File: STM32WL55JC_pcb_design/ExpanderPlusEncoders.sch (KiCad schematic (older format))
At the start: 11 parts, among them IC2 CY8C9540A-24PVXIT, J12 Conn_01x10, J13 Conn_01x10, J14 Conn_01x10, J15 Conn_01x10, SW2 SW_MEC_5E

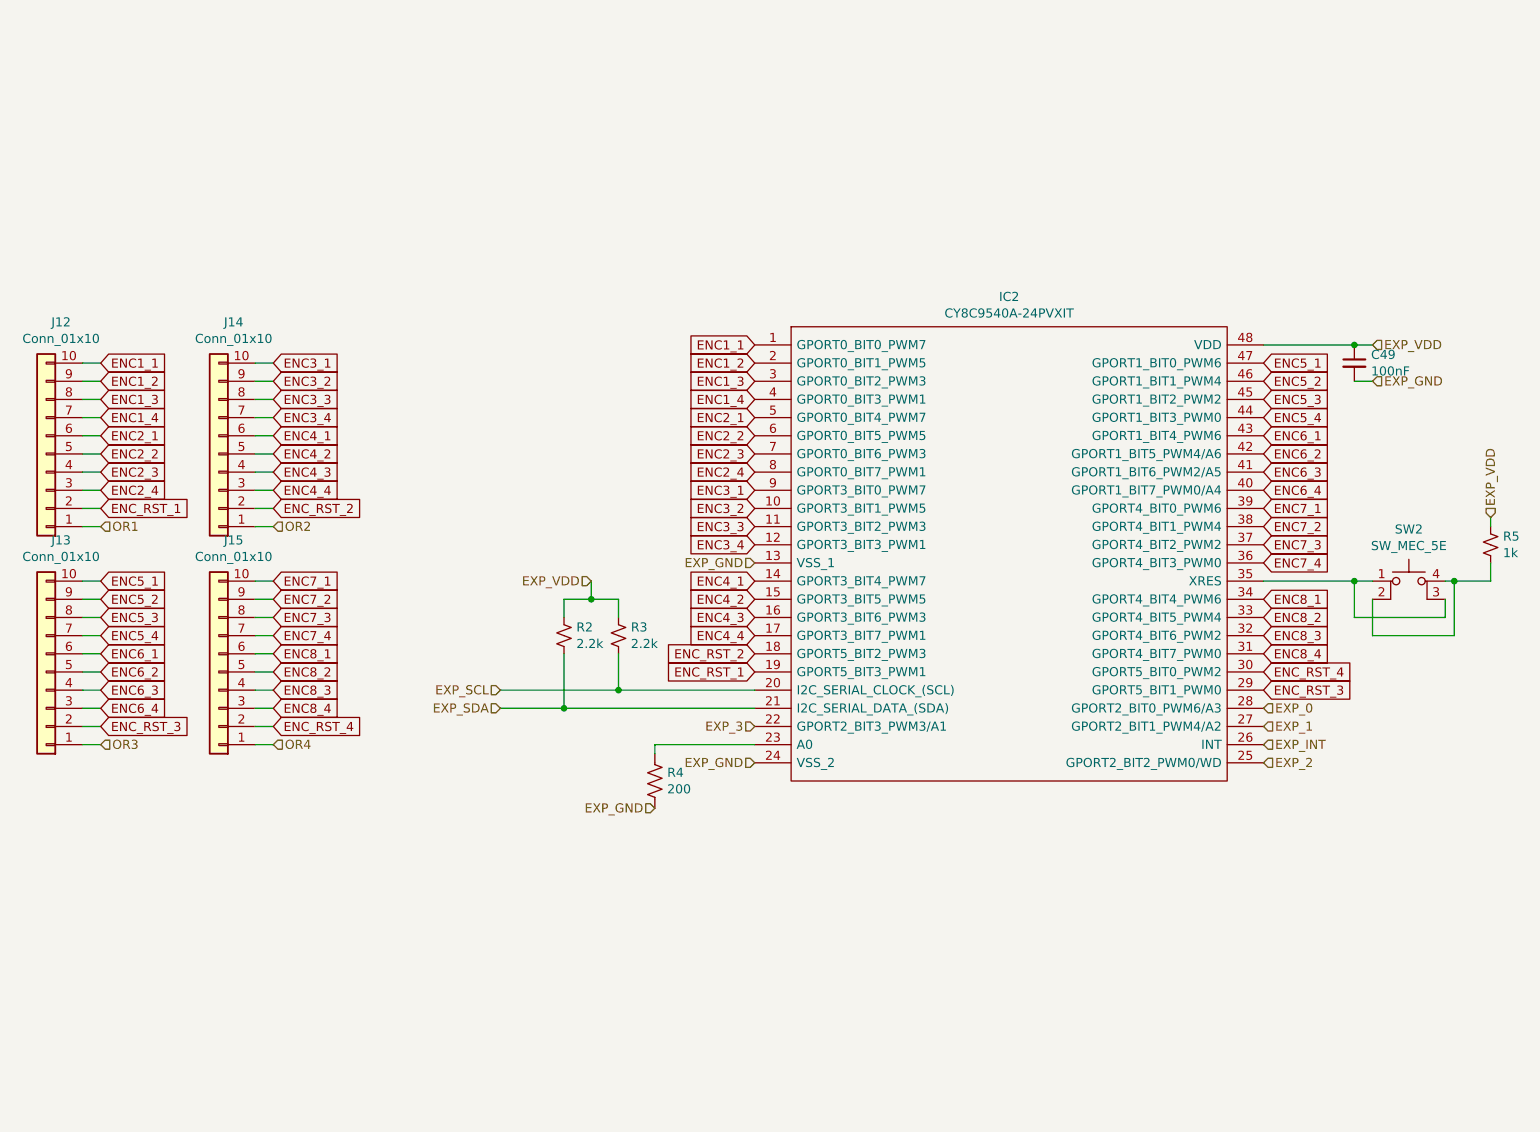
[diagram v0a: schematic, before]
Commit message: Change devices to available ones from JLC
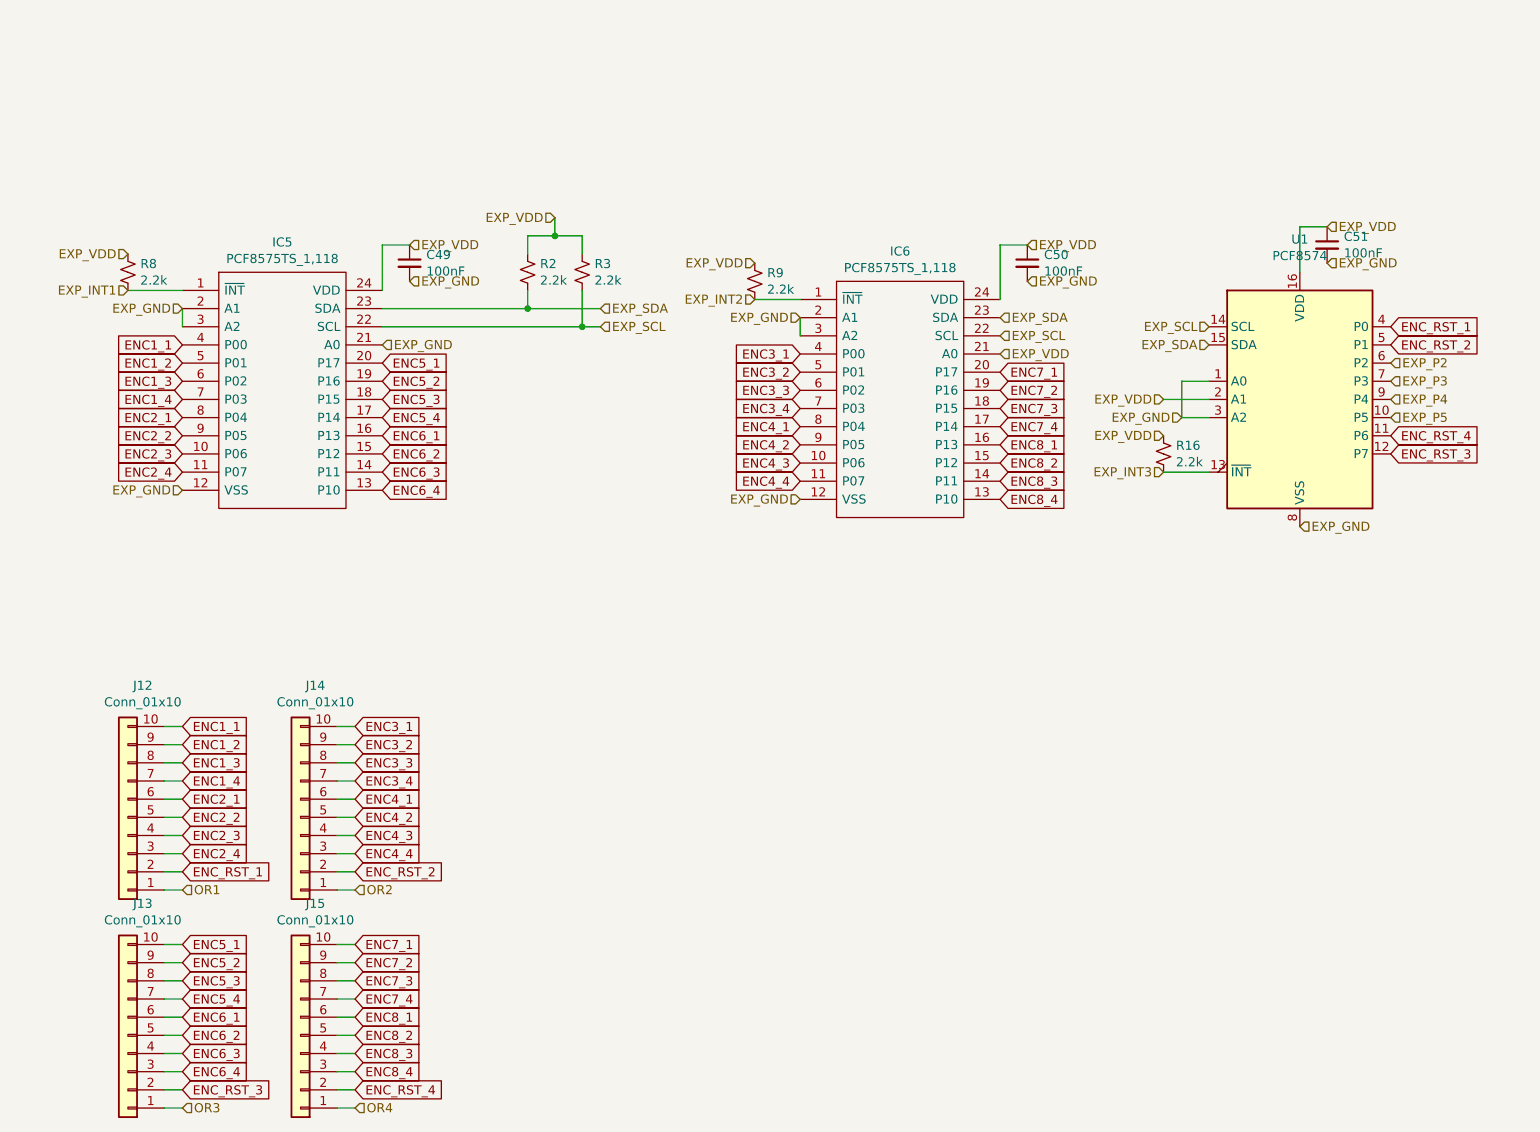
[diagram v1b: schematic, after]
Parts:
- removed IC2: CY8C9540A-24PVXIT, CY8C9540A-24PVXIT:SOP64P1035X279-48N, symbol CY8C9540A-24PVXIT:CY8C9540A-24PVXIT
- removed R4: 200, Resistor_SMD:R_0805_2012Metric, symbol Device:R_US
- removed R5: 1k, Resistor_SMD:R_0805_2012Metric, symbol Device:R_Small_US
- removed SW2: SW_MEC_5E, EVQ-P2F02K:EVQP2V02W, symbol Switch:SW_MEC_5E
- added C50, C51: 100nF, Capacitor_SMD:C_0805_2012Metric, symbol Device:C_Small
- added IC5, IC6: PCF8575TS_1,118, PCF8575TS_1_118:SOP65P775X200-24N, symbol PCF8575TS_1_118:PCF8575TS_1,118
- added R16, R8, R9: 2.2k, Resistor_SMD:R_0805_2012Metric, symbol Device:R_Small_US
- added U1: PCF8574, PCF8574T_3_518:SOIC127P1032X265-16N, symbol Interface_Expansion:PCF8574
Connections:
- net ENC1_1: now also IC5.4 (P00)
- net ENC1_2: now also IC5.5 (P01)
- net ENC1_3: now also IC5.6 (P02)
- net ENC1_4: now also IC5.7 (P03)
- net ENC2_1: now also IC5.8 (P04)
- net ENC2_2: now also IC5.9 (P05)
- net ENC2_3: now also IC5.10 (P06)
- net ENC2_4: now also IC5.11 (P07)
- net ENC3_1: now also IC6.4 (P00)
- net ENC3_2: now also IC6.5 (P01)
- net ENC3_3: now also IC6.6 (P02)
- net ENC3_4: now also IC6.7 (P03)
- net ENC4_1: now also IC6.8 (P04)
- net ENC4_2: now also IC6.9 (P05)
- net ENC4_3: now also IC6.10 (P06)
- net ENC4_4: now also IC6.11 (P07)
- net ENC5_1: now also IC5.20 (P17)
- net ENC5_2: now also IC5.19 (P16)
- net ENC5_3: now also IC5.18 (P15)
- net ENC5_4: now also IC5.17 (P14)
- net ENC6_1: now also IC5.16 (P13)
- net ENC6_2: now also IC5.15 (P12)
- net ENC6_3: now also IC5.14 (P11)
- net ENC6_4: now also IC5.13 (P10)
- net ENC7_1: now also IC6.20 (P17)
- net ENC7_2: now also IC6.19 (P16)
- net ENC7_3: now also IC6.18 (P15)
- net ENC7_4: now also IC6.17 (P14)
- net ENC8_1: now also IC6.16 (P13)
- net ENC8_2: now also IC6.15 (P12)
- net ENC8_3: now also IC6.14 (P11)
- net ENC8_4: now also IC6.13 (P10)
- net ENC_RST_1: now also U1.4 (P0)
- net ENC_RST_2: now also U1.5 (P1)
- net ENC_RST_3: now also U1.12 (P7)
- net ENC_RST_4: now also U1.11 (P6)
- net EXP_GND: now also C50.2, C51.2, IC5.12 (VSS), IC5.2 (A1), IC5.21 (A0), IC5.3 (A2), IC6.12 (VSS), IC6.2 (A1), IC6.3 (A2), U1.1 (A0), U1.3 (A2), U1.8 (VSS)
- net EXP_SCL: now also IC5.22 (SCL), IC6.22 (SCL), U1.14 (SCL)
- net EXP_SDA: now also IC5.23 (SDA), IC6.23 (SDA), U1.15 (SDA)
- net EXP_VDD: now also C50.1, C51.1, IC5.24 (VDD), IC6.21 (A0), IC6.24 (VDD), R16.1, R8.1, R9.1, U1.16 (VDD), U1.2 (A1)
- new net EXP_INT1: IC5.1 (~INT), R8.2
- new net EXP_INT2: IC6.1 (~INT), R9.2
- new net EXP_INT3: R16.2, U1.13 (~INT~)
- new net EXP_P2: U1.6 (P2)
- new net EXP_P3: U1.7 (P3)
- new net EXP_P4: U1.9 (P4)
- new net EXP_P5: U1.10 (P5)
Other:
- moved on the sheet: J12, J13, J14, J15, R2, R3

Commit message: Finish silk screen
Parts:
- added TP5: EXP_VDD1, TestPoint:TestPoint_Pad_D4.0mm, symbol Connector:TestPoint
- added TP7: EXP_VDD3, TestPoint:TestPoint_Pad_D4.0mm, symbol Connector:TestPoint
- added TP8: EXP_GND, TestPoint:TestPoint_Pad_D4.0mm, symbol Connector:TestPoint
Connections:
- net EXP_GND: now also TP8.1
- new net VDD: TP5.1, TP7.1
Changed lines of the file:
@@
 Text HLabel 8700 3400 2    50   Input ~ 0
 EXP_GND
-Text HLabel 5950 3250 0    50   Input ~ 0
+Text HLabel 5800 3250 0    50   Input ~ 0
 EXP_GND
-Text HLabel 2550 3200 0    50   Input ~ 0
+Text HLabel 2400 3200 0    50   Input ~ 0
 EXP_GND
 Wire Wire Line
@@
 Text HLabel 5950 2250 0    50   Input ~ 0
 EXP_GND
+Wire Wire Line
+	2400 3200 2550 3200
+Wire Wire Line
+	5800 3250 5950 3250
+$Comp
+L Connector:TestPoint TP5
+U 1 1 61852EEA
+P 5150 750
+F 0 "TP5" H 5208 868 50  0000 L CNN
+F 1 "EXP_VDD1" H 5208 777 50  0000 L CNN
+F 2 "TestPoint:TestPoint_Pad_D4.0mm" H 5350 750 50  0001 C CNN
+F 3 "~" H 5350 750 50  0001 C CNN
+	1    5150 750
+	1    0    0    -1
+$EndComp
+$Comp
+L Connector:TestPoint TP7
+U 1 1 61853FC4
+P 5600 750
+F 0 "TP7" H 5658 868 50  0000 L CNN
+F 1 "EXP_VDD3" H 5658 777 50  0000 L CNN
+F 2 "TestPoint:TestPoint_Pad_D4.0mm" H 5800 750 50  0001 C CNN
+F 3 "~" H 5800 750 50  0001 C CNN
+	1    5600 750
+	1    0    0    -1
+$EndComp
+$Comp
+L Connector:TestPoint TP8
+U 1 1 618543B9
+P 6050 750
+F 0 "TP8" H 6108 868 50  0000 L CNN
+F 1 "EXP_GND" H 6108 777 50  0000 L CNN
+F 2 "TestPoint:TestPoint_Pad_D4.0mm" H 6250 750 50  0001 C CNN
+F 3 "~" H 6250 750 50  0001 C CNN
+	1    6050 750
+	1    0    0    -1
+$EndComp
+Text GLabel 5150 750  3    50   Input ~ 0
+VDD
+Text GLabel 5600 750  3    50   Input ~ 0
+VDD
+Text HLabel 6050 750  3    50   Input ~ 0
+EXP_GND
 $EndSCHEMATC
